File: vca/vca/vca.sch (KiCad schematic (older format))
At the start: 96 parts, among them U1 TL084, U2 SSI2164, U3 TL084

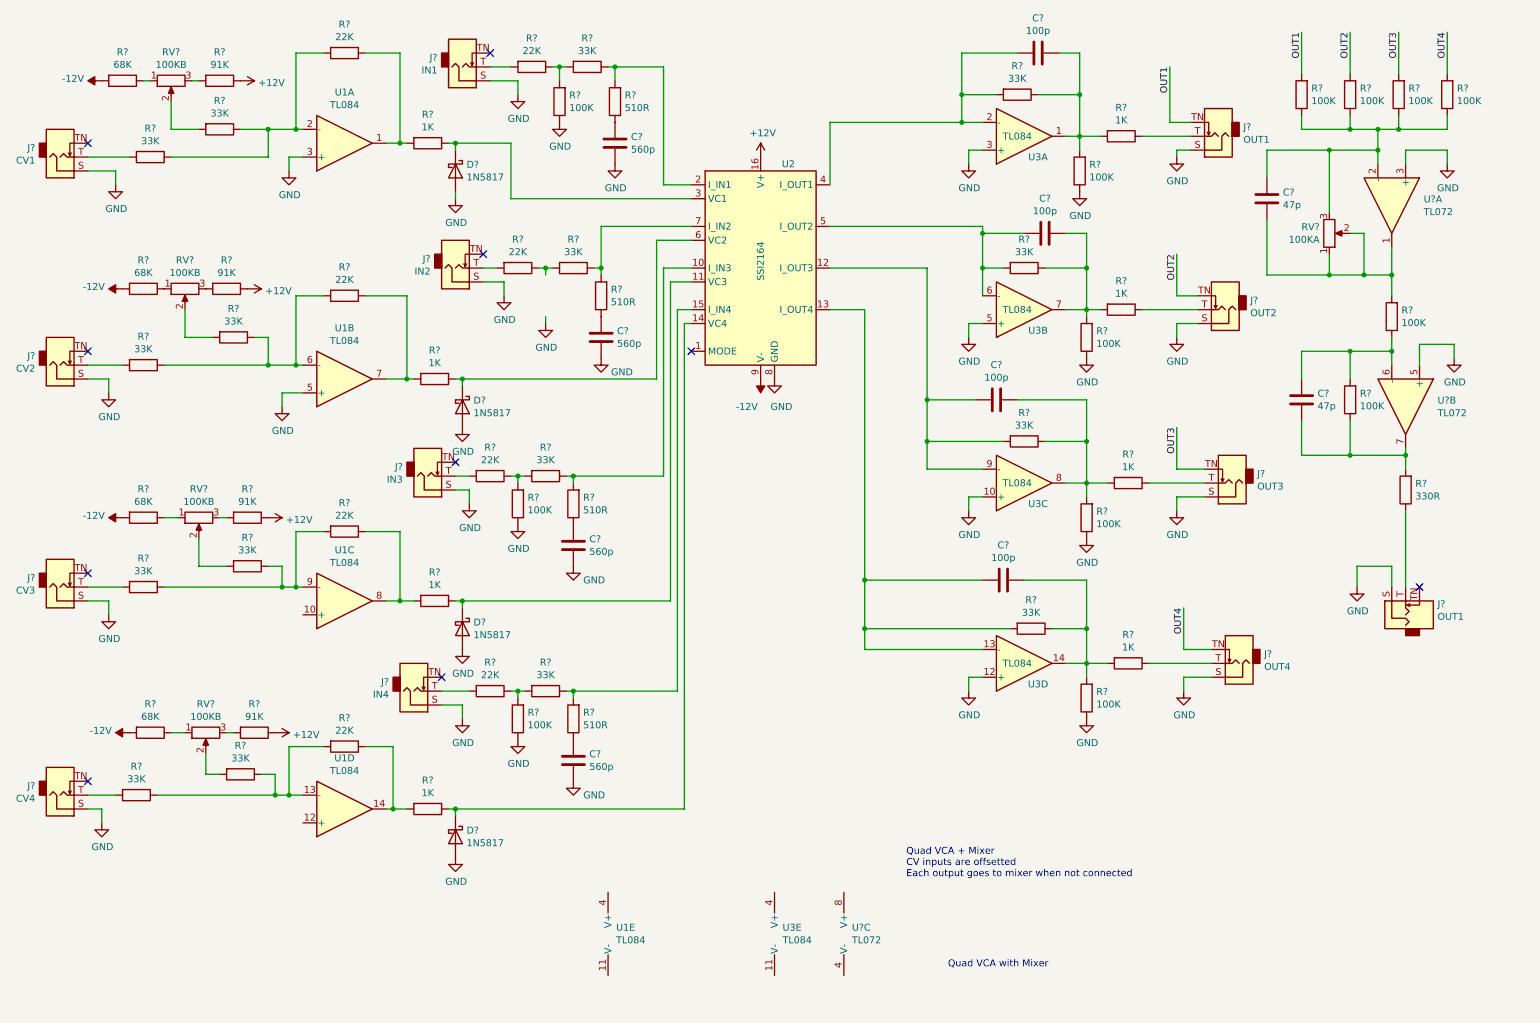
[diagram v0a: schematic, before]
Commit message: Add VCA wip (no lines yet)
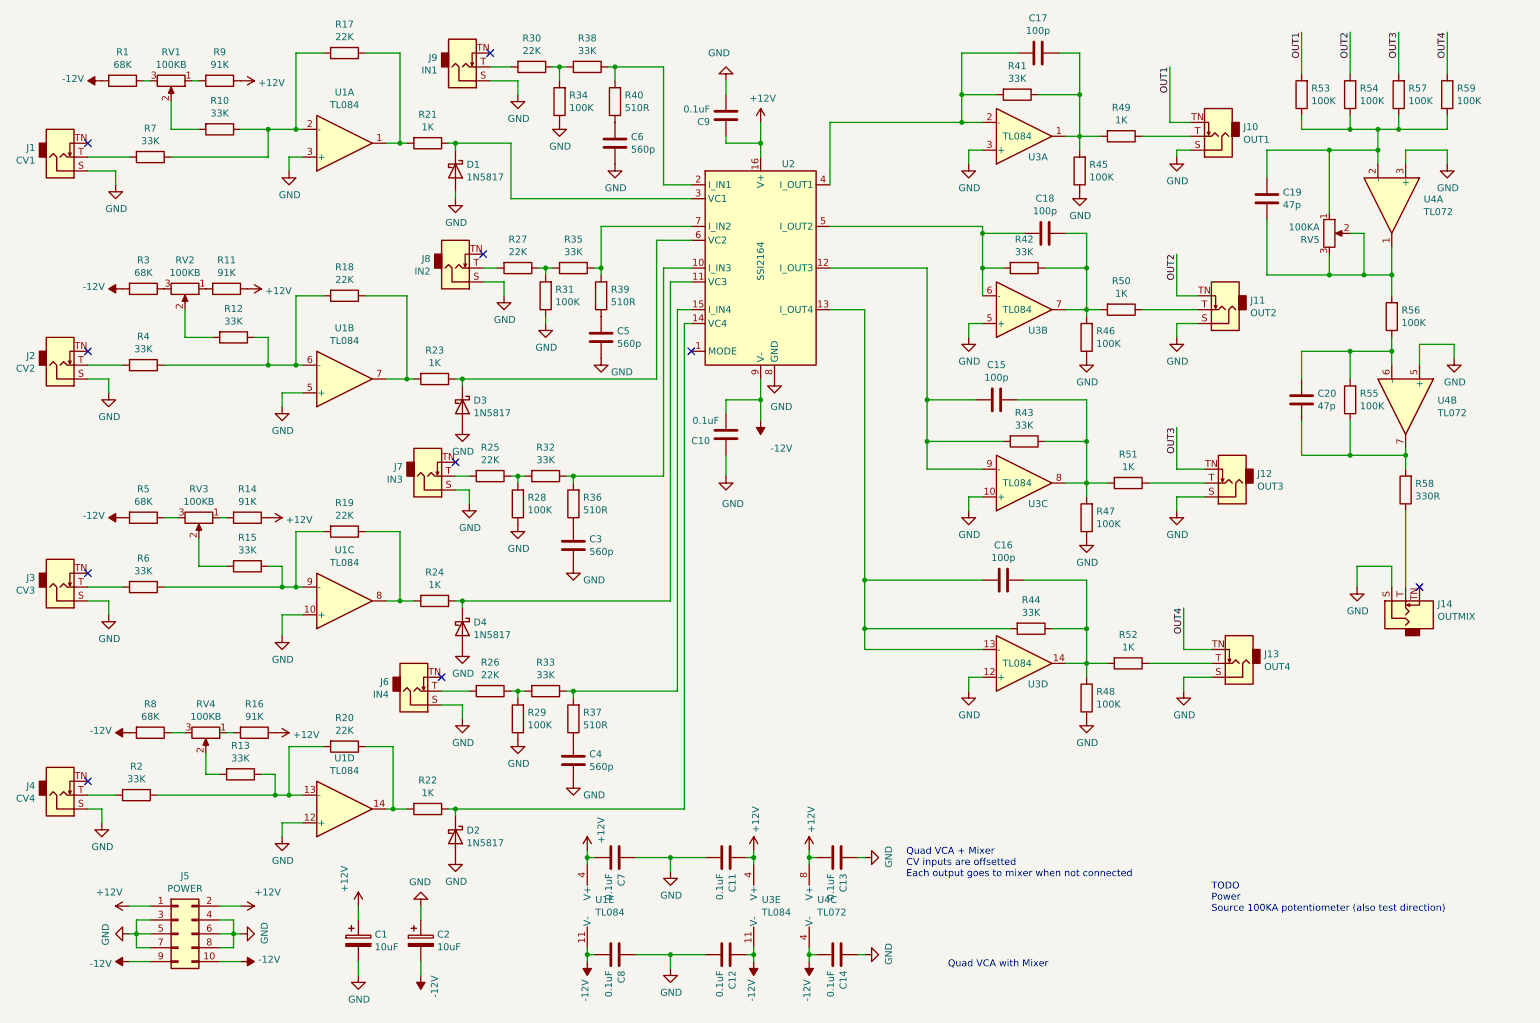
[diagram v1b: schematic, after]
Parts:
- added C1, C2: 10uF, Capacitor_THT:CP_Radial_D5.0mm_P2.50mm, symbol Device:CP
- added C10, C11, C12, C13, C14, C7, C8, C9: 0.1uF, Capacitor_THT:C_Disc_D7.5mm_W2.5mm_P5.00mm, symbol Device:C
- added J5: POWER, Connector_PinHeader_2.54mm:PinHeader_2x05_P2.54mm_Vertical, symbol Connector_Generic:Conn_02x05_Odd_Even
- added R31: 100K, Resistor_THT:R_Axial_DIN0204_L3.6mm_D1.6mm_P7.62mm_Horizontal, symbol Device:R
- C15, C16, C17, C18, C19, C20, C3, C4, C5, C6: renamed from C?; footprint (none) -> Capacitor_THT:C_Disc_D7.5mm_W2.5mm_P5.00mm
- J1, J10, J11, J12, J13, J2, J3, J4, J6, J7, J8, J9: renamed from J?; footprint (none) -> Connector_Audio:Jack_3.5mm_QingPu_WQP-PJ398SM_Vertical_CircularHoles
- J14: renamed from J?; value OUT1 -> OUTMIX; footprint (none) -> Connector_Audio:Jack_3.5mm_QingPu_WQP-PJ398SM_Vertical_CircularHoles
- R1, R10, R11, R12, R13, R14, R15, R16, R17, R18, R19, R2, R20, R21, R22, R23, R24, R25, R26, R27, R28, R29, R3, R30, R32, R33, R34, R35, R36, R37, R38, R39, R4, R40, R41, R42, R43, R44, R45, R46, R47, R48, R49, R5, R50, R51, R52, R53, R54, R55, R56, R57, R58, R59, R6, R7, R8, R9: renamed from R?; footprint (none) -> Resistor_THT:R_Axial_DIN0204_L3.6mm_D1.6mm_P7.62mm_Horizontal
- RV1, RV2, RV3, RV4, RV5: renamed from RV?; footprint (none) -> Potentiometer_THT:Potentiometer_Alps_RK09L_Single_Vertical
- U1, U3: footprint (none) -> Package_DIP:DIP-14_W7.62mm_Socket
- U2: footprint Package_SO:SOIC-16_3.9x9.9mm_P1.27mm -> Package_DIP:DIP-16_W7.62mm_Socket
- U4: renamed from U?; footprint (none) -> Package_DIP:DIP-8_W7.62mm_Socket
- gave numbers to parts that had none: 4
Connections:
- net +12V: now also U1.4 (V+), U3.4 (V+), U4.8 (V+), C1.1, C11.1, C13.2, C7.2, C9.1, J5.1 (Pin_1), J5.2 (Pin_2)
- net -12V: now also U1.11 (V-), U3.11 (V-), U4.4 (V-), C10.2, C12.1, C14.2, C2.2, C8.2, J5.10 (Pin_10), J5.9 (Pin_9)
- net GND: now also U1.10 (+), U1.12 (+), C1.2, C10.1, C11.2, C12.2, C13.1, C14.1, C2.1, C7.1, C8.1, C9.2, J5.3 (Pin_3), J5.4 (Pin_4), J5.5 (Pin_5), J5.6 (Pin_6), J5.7 (Pin_7), J5.8 (Pin_8), R31.1
- net at RV1.1: now also R9.2; no longer R1.1
- net at RV1.3: now also R1.1; no longer R9.2
- net at RV2.1: now also R11.2; no longer R3.1
- net at RV2.3: now also R3.1; no longer R11.2
- net at RV3.1: now also R14.2; no longer R5.1
- net at RV3.3: now also R5.1; no longer R14.2
- net at RV4.1: now also R16.2; no longer R8.1
- net at RV4.3: now also R8.1; no longer R16.2
- net at R27.1, R35.2: now also R31.2
- net at C19.1, R56.2, RV5.2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: now also RV5.3; no longer RV5.1
- net at C19.2, R53.1, R54.1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: now also RV5.1; no longer RV5.3
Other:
- note added: "TODO\nPower\nSource 100KA potentiometer (also test direction)"
- moved on the sheet: U1E, U3E, U4C

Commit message: Add VCA panel plus noise module
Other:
- note removed: "TODO\nPower\nSource 100KA potentiometer (also test direction)"
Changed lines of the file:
@@
 Text Notes 7350 7500 0    50   ~ 0
 Quad VCA with Mixer
-Text Notes 9250 7100 0    50   ~ 0
-TODO\nPower\nSource 100KA potentiometer (also test direction)
 $Comp
 L power:GND #PWR020
